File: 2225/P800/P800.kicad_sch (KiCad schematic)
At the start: 25 parts, among them J801 Screw_Terminal_01x04, J802 Screw_Terminal_01x08

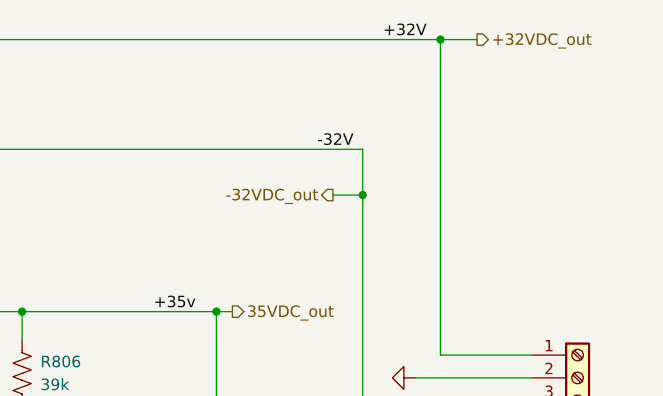
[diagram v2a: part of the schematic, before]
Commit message: Added dummy power inputs to P700 block in 2225.kicad_sch (system block diagram)
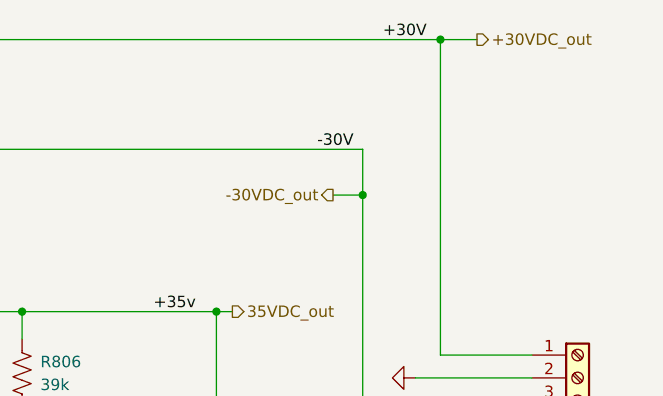
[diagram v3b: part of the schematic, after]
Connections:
- net +32VDC_out renamed +30VDC_out
- net -32VDC_out renamed -30VDC_out
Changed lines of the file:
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@@
     (effects (font (size 1.27 1.27)) (justify right bottom))
   )
-  (label "-32V" (at 231.394 65.786 180)
+  (label "-30V" (at 231.394 65.786 180)
     (effects (font (size 1.27 1.27)) (justify right bottom))
   )
-  (label "+32V" (at 239.522 53.594 180)
+  (label "+30V" (at 239.522 53.594 180)
     (effects (font (size 1.27 1.27)) (justify right bottom))
   )
@@
     (effects (font (size 1.27 1.27)) (justify right))
   )
-  (hierarchical_label "-32VDC_out" (shape output) (at 229.108 70.866 180)
+  (hierarchical_label "-30VDC_out" (shape output) (at 229.108 70.866 180)
     (effects (font (size 1.27 1.27)) (justify right))
   )
-  (hierarchical_label "+32VDC_out" (shape output) (at 245.11 53.594 0)
+  (hierarchical_label "+30VDC_out" (shape output) (at 245.11 53.594 0)
     (effects (font (size 1.27 1.27)) (justify left))
   )

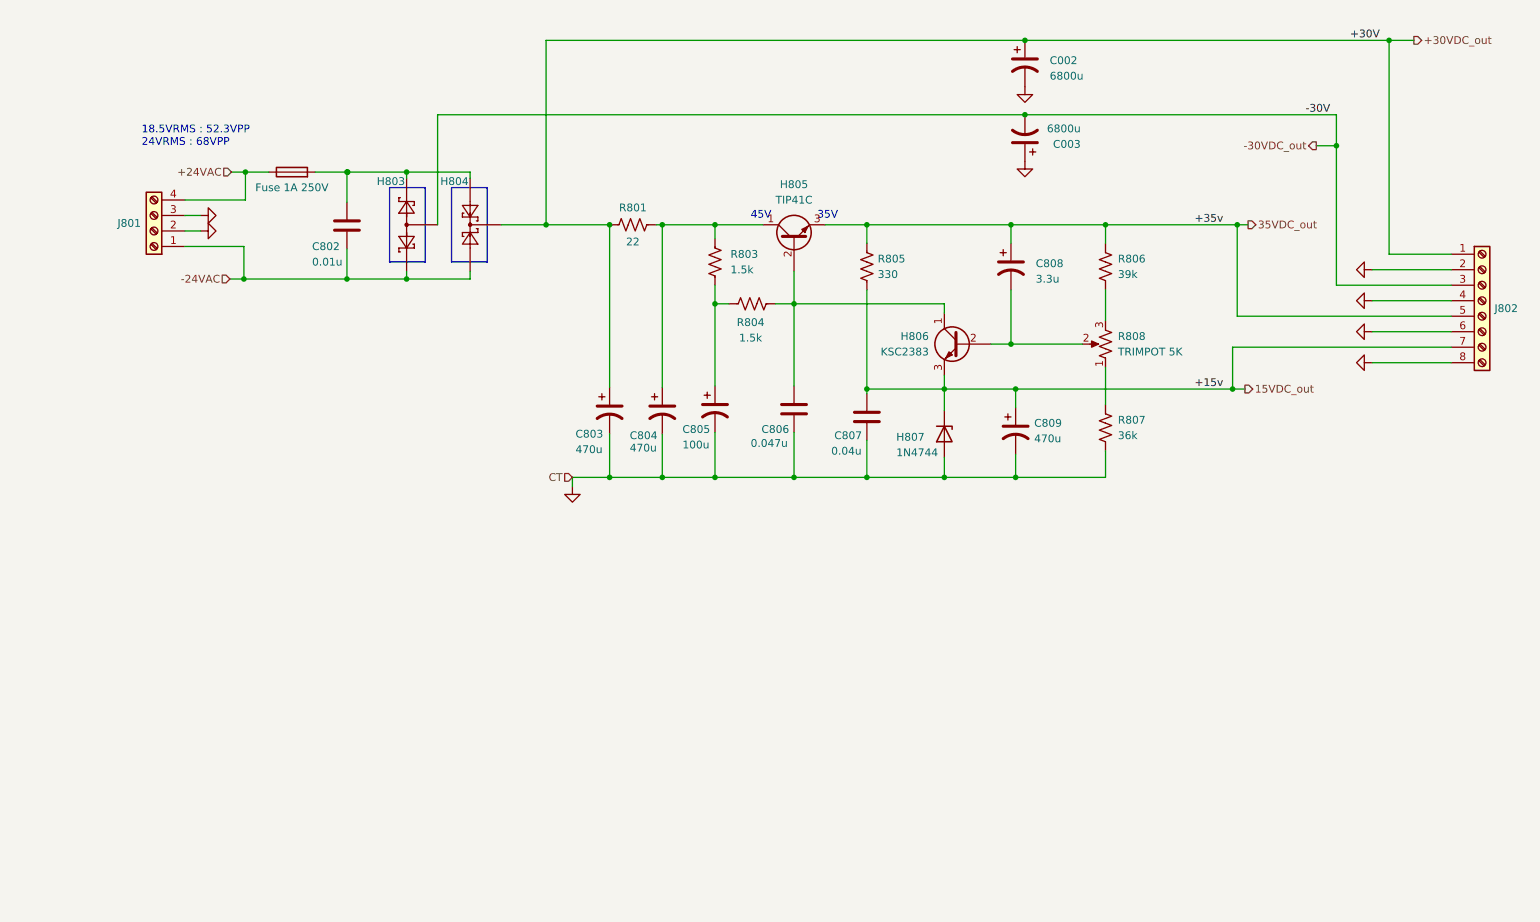
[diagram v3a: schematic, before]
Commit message: Updated terminal connectors in 2225/P800/P800.kicad_sch
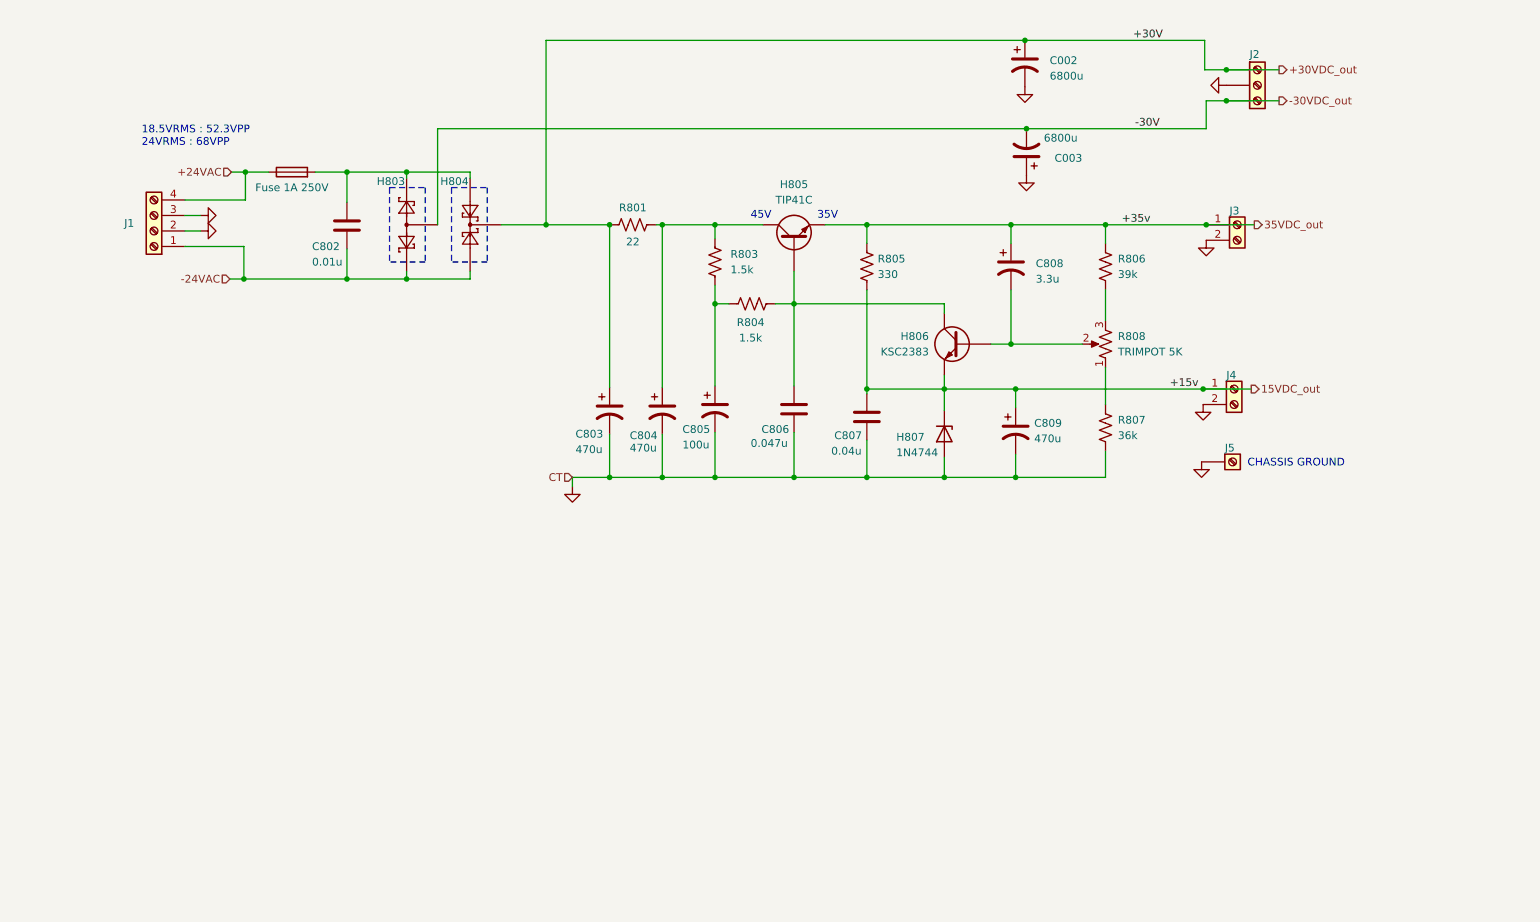
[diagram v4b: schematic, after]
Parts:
- removed J802: Screw_Terminal_01x08, symbol Connector:Screw_Terminal_01x08
- added J2: Screw_Terminal_01x03, symbol Connector:Screw_Terminal_01x03
- added J3, J4: Screw_Terminal_01x02, symbol Connector:Screw_Terminal_01x02
- added J5: Screw_Terminal_01x01, symbol Connector:Screw_Terminal_01x01
- F1: Spice_Model 1u -> (none); Spice_Netlist_Enabled Y -> (none); Spice_Primitive R -> (none)
- H803: Spice_Lib_File ${KIPRJMOD}/../models/P800/P800.lib -> (none); Spice_Model DIODE_PAIR_CA -> (none); Spice_Netlist_Enabled Y -> (none); Spice_Primitive X -> (none)
- H804: Spice_Lib_File ${KIPRJMOD}/../models/P800/P800.lib -> (none); Spice_Model DIODE_PAIR_CC -> (none); Spice_Netlist_Enabled Y -> (none); Spice_Primitive X -> (none)
- H805: Spice_Lib_File ${KIPRJMOD}/../models/P800/P800.lib -> (none); Spice_Model TIP41C -> (none); Spice_Netlist_Enabled Y -> (none); Spice_Primitive Q -> (none)
- H806: Spice_Lib_File ${KIPRJMOD}/../models/P800/P800.lib -> (none); Spice_Model KSC2383 -> (none); Spice_Netlist_Enabled Y -> (none); Spice_Primitive Q -> (none)
- H807: Spice_Lib_File ${KIPRJMOD}/../models/P800/P800.lib -> (none); Spice_Model D1N4744A -> (none); Spice_Netlist_Enabled Y -> (none); Spice_Node_Sequence 2 1 -> (none); Spice_Primitive D -> (none)
- J1: renamed from J801; Spice_Model Screw_Terminal_01x04 -> (none); Spice_Netlist_Enabled N -> (none); Spice_Primitive J -> (none)
- R801: footprint (none) -> Resistor_THT:R_Axial_DIN0414_L11.9mm_D4.5mm_P15.24mm_Horizontal; Spice_Model 22 -> (none); Spice_Netlist_Enabled Y -> (none); Spice_Primitive R -> (none)
- R803, R804, R806, R807: footprint (none) -> Resistor_THT:R_Axial_DIN0207_L6.3mm_D2.5mm_P7.62mm_Horizontal
- R805: footprint (none) -> Resistor_THT:R_Axial_DIN0414_L11.9mm_D4.5mm_P15.24mm_Horizontal
- R808: Spice_Lib_File ${KIPRJMOD}/../models/P800/P800.lib -> (none); Spice_Model LINEAR_POTENTIOMETER POT_VAL=5k SET=0.62 -> (none); Spice_Netlist_Enabled Y -> (none); Spice_Primitive X -> (none)
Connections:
- net +30VDC_out: now also J2.1 (Pin_1)
- net -30VDC_out: now also J2.3 (Pin_3)
- net 15VDC_out: now also J4.1 (Pin_1)
- net 35VDC_out: now also J3.1 (Pin_1)
- net GND: now also J2.2 (Pin_2), J3.2 (Pin_2), J4.2 (Pin_2), J5.1 (Pin_1)
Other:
- note added: "CHASSIS GROUND"
- moved on the sheet: C003

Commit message: Aligned 2225/P800 schematic elements to grid so ERC would run without warnings. Deconflicted net names. Fixed warning about GND having been modified in PWR library.
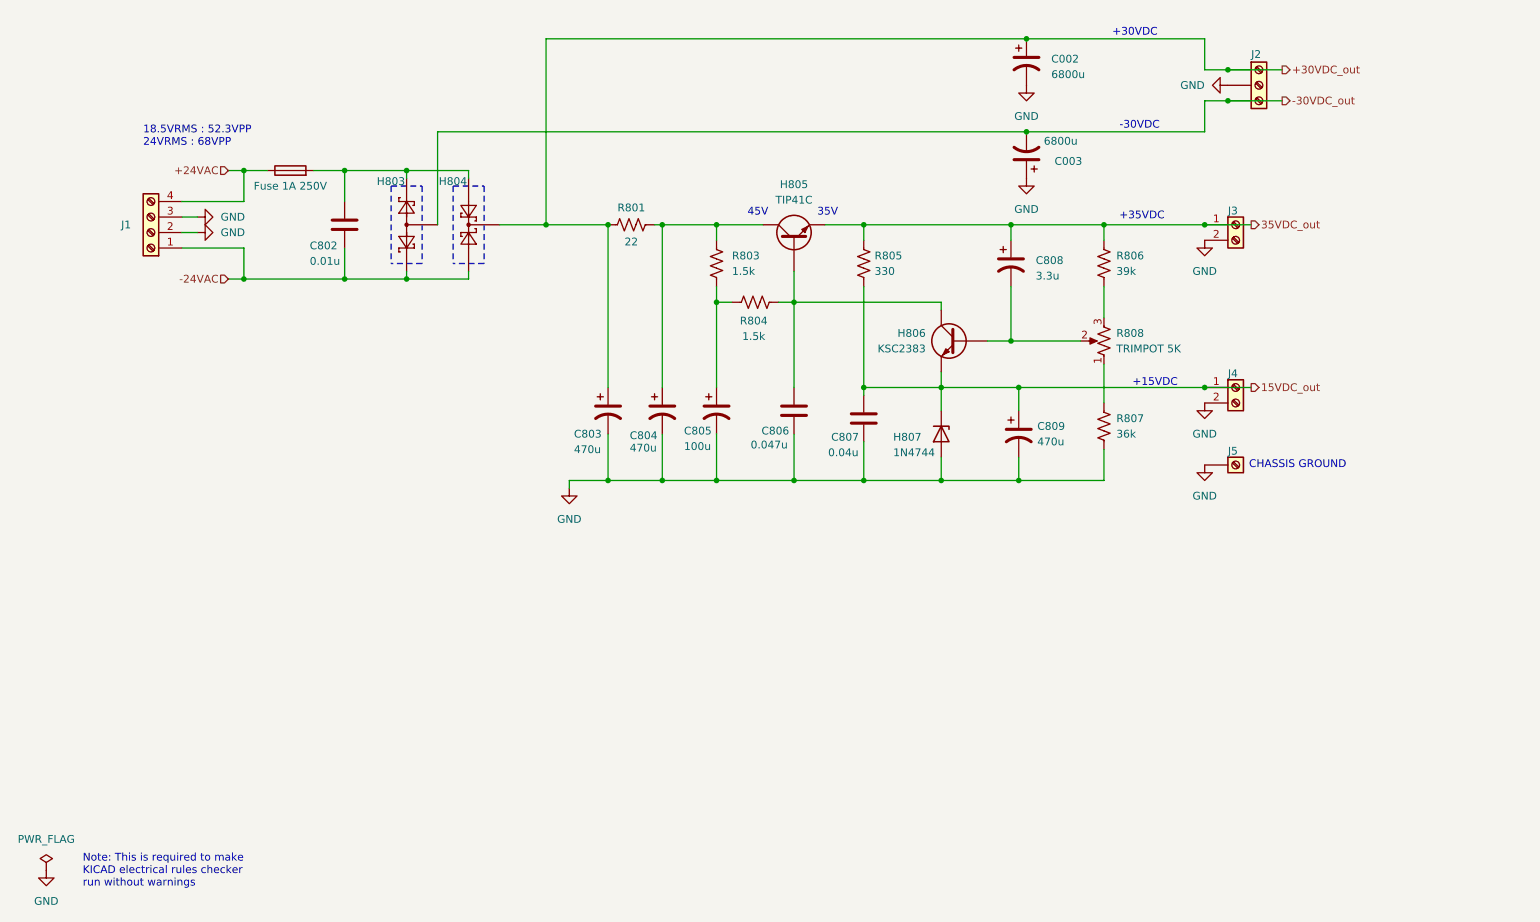
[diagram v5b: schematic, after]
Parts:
- J2: footprint (none) -> P800_footprint_library:molex_3pos_connector_393570003
- J3, J4: footprint (none) -> P800_footprint_library:molex_2pos_connector_393570002
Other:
- note added: "+15VDC"
- note added: "+30VDC"
- note added: "+35VDC"
- note added: "-30VDC"
- note added: "Note: This is required to make KICAD electrical rules checker run without warnings"
- moved on the sheet: C003, C807, C808, C809, H806, H807, J1, J5, R804, R805, R806, R808

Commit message: Made and populated 2225/P800/3dmodels and libs. Created project footprint library for 2225/P800. Added molex connector foorptints to 2225/P800 library.
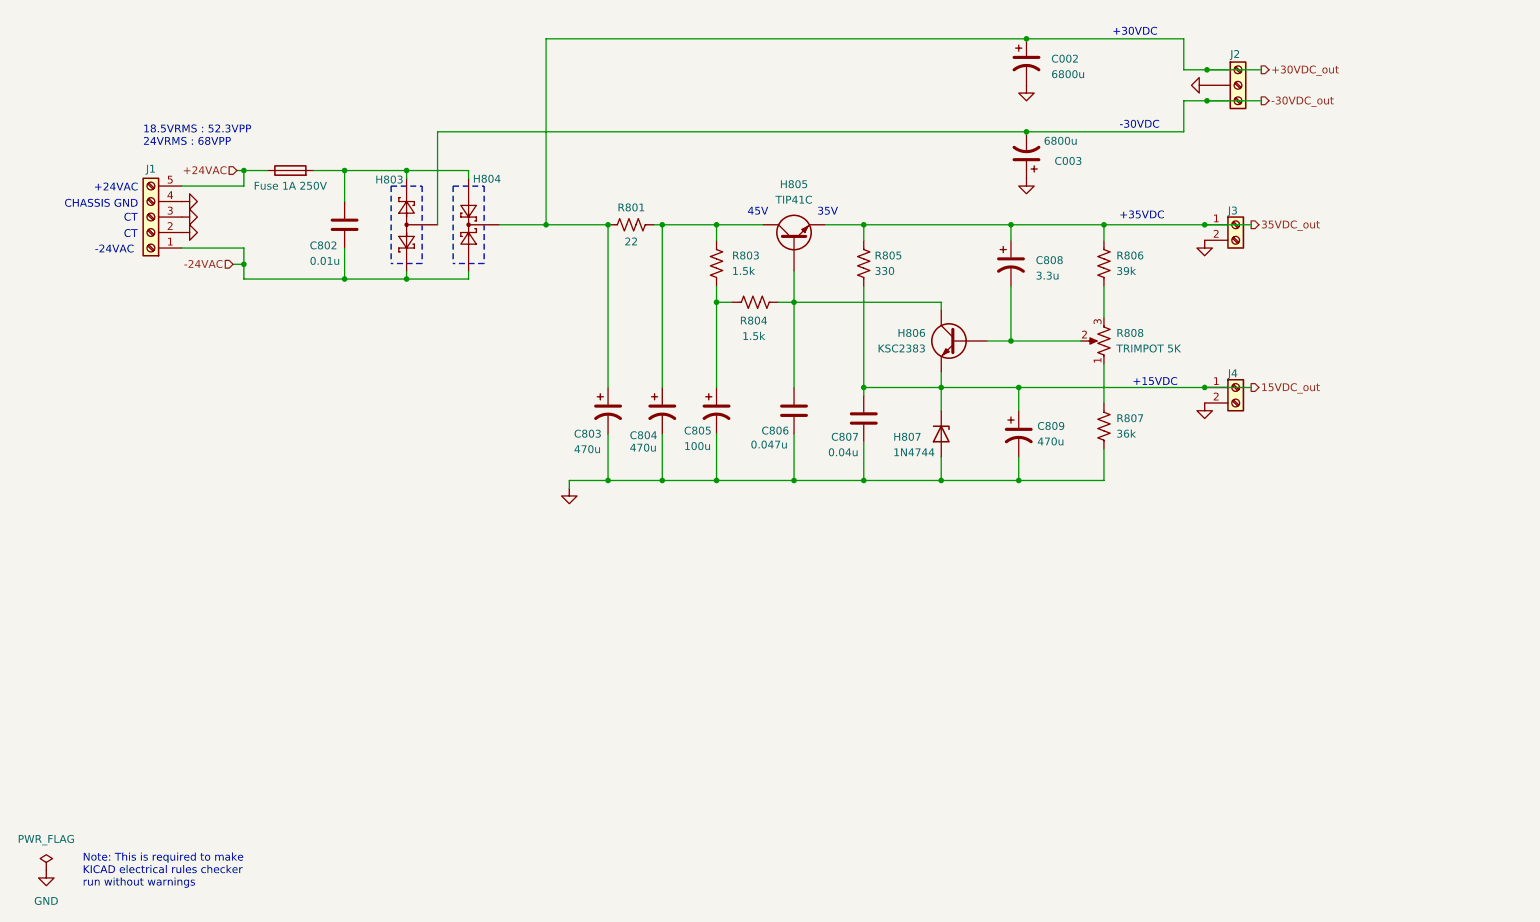
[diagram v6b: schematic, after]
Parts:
- removed J1: Screw_Terminal_01x04, symbol Connector:Screw_Terminal_01x04
- removed J5: Screw_Terminal_01x01, symbol Connector:Screw_Terminal_01x01
- added J1: Screw_Terminal_01x05, P800_footprint_library:molex_5pos_connector_395443005, symbol Connector:Screw_Terminal_01x05
- R801, R805: footprint Resistor_THT:R_Axial_DIN0414_L11.9mm_D4.5mm_P15.24mm_Horizontal -> (none)
- R803, R804, R806, R807: footprint Resistor_THT:R_Axial_DIN0207_L6.3mm_D2.5mm_P7.62mm_Horizontal -> (none)
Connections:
- net +24VAC: now also J1.5 (Pin_5)
- net -24VAC: now also J1.1 (Pin_1)
- net GND: now also J1.2 (Pin_2), J1.3 (Pin_3), J1.4 (Pin_4)
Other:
- note added: "+24VAC"
- note added: "-24VAC"
- note added: "CHASSIS GND"
- note added: "CT"
- note removed: "CHASSIS GROUND"
- moved on the sheet: J2

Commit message: Changed molex block connectors for all VDC_out to SMA right angle THT. Aligned schematic to 50.0 mil grid to fix electrical rules checker warnings.
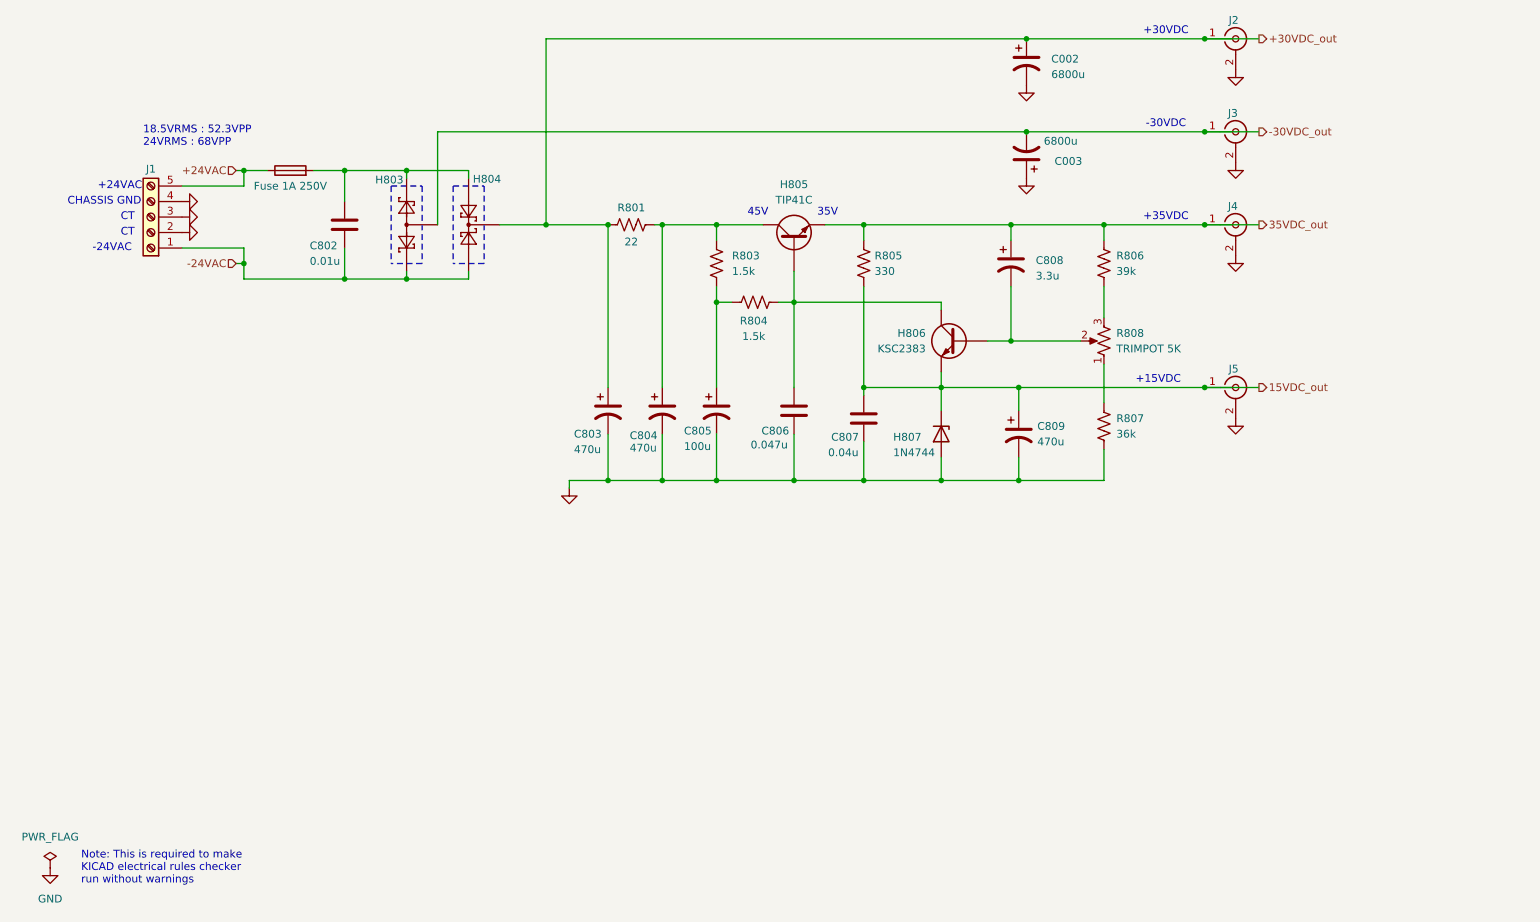
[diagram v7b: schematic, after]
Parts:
- removed J2: Screw_Terminal_01x03, P800_footprint_library:molex_3pos_connector_393570003, symbol Connector:Screw_Terminal_01x03
- removed J3, J4: Screw_Terminal_01x02, P800_footprint_library:molex_2pos_connector_393570002, symbol Connector:Screw_Terminal_01x02
- added J2, J3, J4, J5: Conn_Coaxial, P800_footprint_library:GRADCONN_RFPC-SMA27-F, symbol Connector:Conn_Coaxial
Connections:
- net +30VDC_out: now also J2.1 (In)
- net -30VDC_out: now also J3.1 (In)
- net 15VDC_out: now also J5.1 (In)
- net 35VDC_out: now also J4.1 (In)
- net GND: now also J2.2 (Ext), J3.2 (Ext), J4.2 (Ext), J5.2 (Ext)
